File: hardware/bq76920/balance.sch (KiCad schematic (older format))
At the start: 35 parts, among them Q4 NTR3C21NZ, Q5 NTR3C21NZ, Q6 NTR3C21NZ, Q7 NTR3C21NZ, Q8 NTR3C21NZ

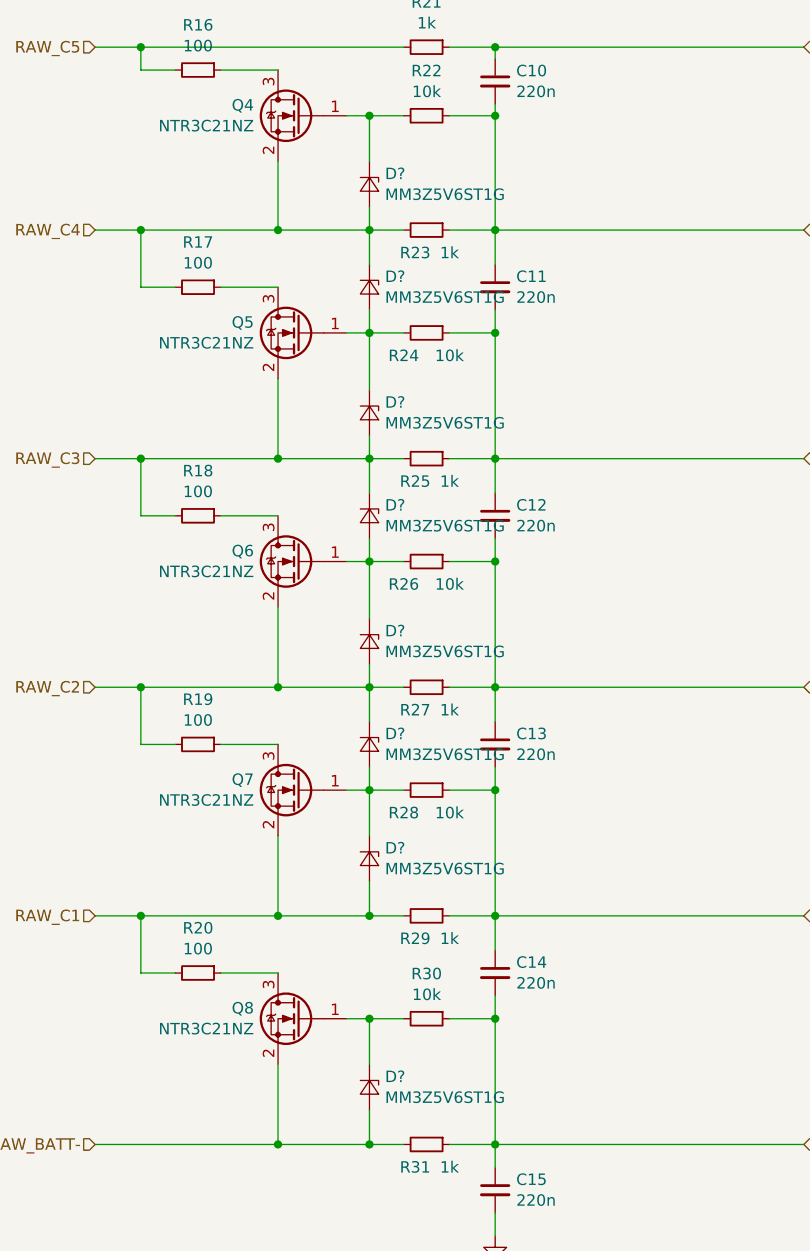
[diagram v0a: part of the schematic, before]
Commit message: clean up, adnotate, footprints
Signed-off-by: Ene Alexandru <ene.alexandru@gmail.com>
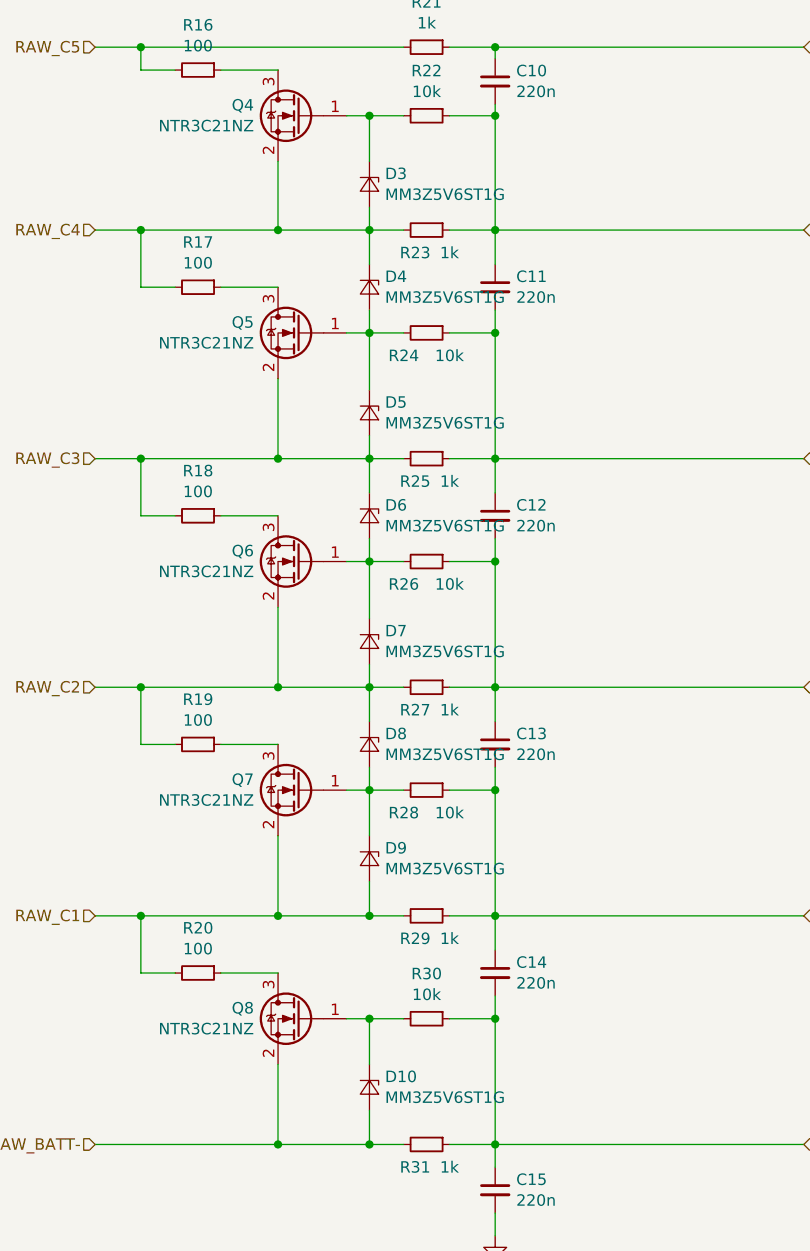
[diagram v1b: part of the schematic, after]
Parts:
- D10, D3, D4, D5, D6, D7, D8: renamed from D?; footprint Diode_SMD:D_SOD-323 -> Diode_SMD:D_SOD-323_HandSoldering
- gave numbers to parts that had none: 1
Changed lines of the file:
@@
 cell balance section
 $Comp
-L Device:D_Zener_Small D?
+L Device:D_Zener_Small D3
 U 1 1 5E152DFD
 P 3700 1450
-F 0 "D?" V 3654 1518 50  0000 L CNN
+F 0 "D3" V 3654 1518 50  0000 L CNN
 F 1 "MM3Z5V6ST1G" V 3745 1518 50  0000 L CNN
-F 2 "Diode_SMD:D_SOD-323" V 3700 1450 50  0001 C CNN
+F 2 "Diode_SMD:D_SOD-323_HandSoldering" V 3700 1450 50  0001 C CNN
 F 3 "~" V 3700 1450 50  0001 C CNN
 	1    3700 1450
@@
 $EndComp
 $Comp
-L Device:D_Zener_Small D?
+L Device:D_Zener_Small D4
 U 1 1 5E1532E1
 P 3700 1900
-F 0 "D?" V 3654 1968 50  0000 L CNN
+F 0 "D4" V 3654 1968 50  0000 L CNN
 F 1 "MM3Z5V6ST1G" V 3745 1968 50  0000 L CNN
-F 2 "Diode_SMD:D_SOD-323" V 3700 1900 50  0001 C CNN
+F 2 "Diode_SMD:D_SOD-323_HandSoldering" V 3700 1900 50  0001 C CNN
 F 3 "~" V 3700 1900 50  0001 C CNN
 	1    3700 1900
@@
 $EndComp
 $Comp
-L Device:D_Zener_Small D?
+L Device:D_Zener_Small D5
 U 1 1 5E1533AC
 P 3700 2450
-F 0 "D?" V 3654 2518 50  0000 L CNN
+F 0 "D5" V 3654 2518 50  0000 L CNN
 F 1 "MM3Z5V6ST1G" V 3745 2518 50  0000 L CNN
-F 2 "Diode_SMD:D_SOD-323" V 3700 2450 50  0001 C CNN
+F 2 "Diode_SMD:D_SOD-323_HandSoldering" V 3700 2450 50  0001 C CNN
 F 3 "~" V 3700 2450 50  0001 C CNN
 	1    3700 2450
@@
 $EndComp
 $Comp
-L Device:D_Zener_Small D?
+L Device:D_Zener_Small D6
 U 1 1 5E153406
 P 3700 2900
-F 0 "D?" V 3654 2968 50  0000 L CNN
+F 0 "D6" V 3654 2968 50  0000 L CNN
 F 1 "MM3Z5V6ST1G" V 3745 2968 50  0000 L CNN
-F 2 "Diode_SMD:D_SOD-323" V 3700 2900 50  0001 C CNN
+F 2 "Diode_SMD:D_SOD-323_HandSoldering" V 3700 2900 50  0001 C CNN
 F 3 "~" V 3700 2900 50  0001 C CNN
 	1    3700 2900
@@
 $EndComp
 $Comp
-L Device:D_Zener_Small D?
+L Device:D_Zener_Small D8
 U 1 1 5E15346A
 P 3700 3900
-F 0 "D?" V 3654 3968 50  0000 L CNN
+F 0 "D8" V 3654 3968 50  0000 L CNN
 F 1 "MM3Z5V6ST1G" V 3745 3968 50  0000 L CNN
-F 2 "Diode_SMD:D_SOD-323" V 3700 3900 50  0001 C CNN
+F 2 "Diode_SMD:D_SOD-323_HandSoldering" V 3700 3900 50  0001 C CNN
 F 3 "~" V 3700 3900 50  0001 C CNN
 	1    3700 3900
@@
 $EndComp
 $Comp
-L Device:D_Zener_Small D?
+L Device:D_Zener_Small D9
 U 1 1 5E1535C6
 P 3700 4400
-F 0 "D?" V 3654 4468 50  0000 L CNN
+F 0 "D9" V 3654 4468 50  0000 L CNN
 F 1 "MM3Z5V6ST1G" V 3745 4468 50  0000 L CNN
 F 2 "Diode_SMD:D_SOD-323" V 3700 4400 50  0001 C CNN
@@
 $EndComp
 $Comp
-L Device:D_Zener_Small D?
+L Device:D_Zener_Small D10
 U 1 1 5E153630
 P 3700 5400
-F 0 "D?" V 3654 5468 50  0000 L CNN
+F 0 "D10" V 3654 5468 50  0000 L CNN
 F 1 "MM3Z5V6ST1G" V 3745 5468 50  0000 L CNN
-F 2 "Diode_SMD:D_SOD-323" V 3700 5400 50  0001 C CNN
+F 2 "Diode_SMD:D_SOD-323_HandSoldering" V 3700 5400 50  0001 C CNN
 F 3 "~" V 3700 5400 50  0001 C CNN
 	1    3700 5400
@@
 	3700 3800 3700 3650
 $Comp
-L Device:D_Zener_Small D?
+L Device:D_Zener_Small D7
 U 1 1 5E16355C
 P 3700 3450
-F 0 "D?" V 3654 3518 50  0000 L CNN
+F 0 "D7" V 3654 3518 50  0000 L CNN
 F 1 "MM3Z5V6ST1G" V 3745 3518 50  0000 L CNN
-F 2 "Diode_SMD:D_SOD-323" V 3700 3450 50  0001 C CNN
+F 2 "Diode_SMD:D_SOD-323_HandSoldering" V 3700 3450 50  0001 C CNN
 F 3 "~" V 3700 3450 50  0001 C CNN
 	1    3700 3450

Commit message: final pcb version
Signed-off-by: Ene Alexandru <ene.alexandru@gmail.com>
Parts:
- removed D4, D6, D8: MM3Z5V6ST1G, Diode_SMD:D_SOD-323_HandSoldering, symbol Device:D_Zener_Small
- D9: footprint Diode_SMD:D_SOD-323 -> Diode_SMD:D_SOD-323_HandSoldering
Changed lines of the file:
@@
-$EndComp
-$Comp
-L Device:D_Zener_Small D4
-U 1 1 5E1532E1
-P 3700 1900
-F 0 "D4" V 3654 1968 50  0000 L CNN
-F 1 "MM3Z5V6ST1G" V 3745 1968 50  0000 L CNN
-F 2 "Diode_SMD:D_SOD-323_HandSoldering" V 3700 1900 50  0001 C CNN
-F 3 "~" V 3700 1900 50  0001 C CNN
-	1    3700 1900
-	0    1    1    0
 $EndComp
 $Comp
@@
 $EndComp
 $Comp
-L Device:D_Zener_Small D6
-U 1 1 5E153406
-P 3700 2900
-F 0 "D6" V 3654 2968 50  0000 L CNN
-F 1 "MM3Z5V6ST1G" V 3745 2968 50  0000 L CNN
-F 2 "Diode_SMD:D_SOD-323_HandSoldering" V 3700 2900 50  0001 C CNN
-F 3 "~" V 3700 2900 50  0001 C CNN
-	1    3700 2900
-	0    1    1    0
-$EndComp
-$Comp
-L Device:D_Zener_Small D8
-U 1 1 5E15346A
-P 3700 3900
-F 0 "D8" V 3654 3968 50  0000 L CNN
-F 1 "MM3Z5V6ST1G" V 3745 3968 50  0000 L CNN
-F 2 "Diode_SMD:D_SOD-323_HandSoldering" V 3700 3900 50  0001 C CNN
-F 3 "~" V 3700 3900 50  0001 C CNN
-	1    3700 3900
-	0    1    1    0
-$EndComp
-$Comp
 L Device:D_Zener_Small D9
 U 1 1 5E1535C6
@@
 F 0 "D9" V 3654 4468 50  0000 L CNN
 F 1 "MM3Z5V6ST1G" V 3745 4468 50  0000 L CNN
-F 2 "Diode_SMD:D_SOD-323" V 3700 4400 50  0001 C CNN
+F 2 "Diode_SMD:D_SOD-323_HandSoldering" V 3700 4400 50  0001 C CNN
 F 3 "~" V 3700 4400 50  0001 C CNN
 	1    3700 4400
@@
 Wire Wire Line
 	3700 4100 3700 4300
-Wire Wire Line
-	3700 4000 3700 4100
-Wire Wire Line
-	3700 3800 3700 3650
 $Comp
 L Device:D_Zener_Small D7
@@
 	3700 3100 3700 3350
 Wire Wire Line
-	3700 3000 3700 3100
-Wire Wire Line
-	3700 2800 3700 2650
-Wire Wire Line
 	3700 2100 3700 2350
 Wire Wire Line
-	3700 2000 3700 2100
-Wire Wire Line
-	3700 1800 3700 1650
-Wire Wire Line
 	3700 1550 3700 1650
